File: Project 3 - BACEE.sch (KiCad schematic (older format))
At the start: 13 parts, among them U1 DS1337S, U2 24LC1025, U3 24LC1025, U4 ATMEGA328P-AU, Y1 Crystal 32 MHz, Y2 Crystal 16 MHz

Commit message: Completed wiring in root sheet
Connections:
- net GND is gone; now on net GNDPWR: U4.21 (GND), U4.3 (GND), U4.5 (GND)
- net RESET: now also R2.1
- net SCK: now also D1.2 (A), U1.6 (SCL), U2.6 (SCL), U3.6 (SCL)
- net SDA: now also U1.5 (SDA), U2.5 (SDA), U3.5 (SDA)
- net VCC: now also BT1.1 (+), C3.1, R2.2, U1.3 (INTA), U1.8 (VCC), U2.3 (A2), U2.8 (VCC), U3.3 (A2), U3.8 (VCC), U4.20 (AREF)
- net GNDPWR: now reaches BT1.2 (-)
- net GNDPWR: now also C1.1, C2.1, C3.2, R1.2, U1.4 (GND), U2.4 (GND), U2.7 (WP), U3.4 (GND), U3.7 (WP)
- net at C1.2: now also U4.7 (PB6), Y2.2
- net at C2.2: now also U4.8 (PB7), Y2.1
- net at D1.1 (K): now also R1.1
- net ADDS1: now reaches U3.1 (A0)
- net ADDS1: now also U2.1 (A0), U4.23 (PC0)
- net ADDS2: now reaches U3.2 (A1)
- net ADDS2: now also U2.2 (A1), U4.24 (PC1)
- net SCL: now reaches U4.26 (PC3)
- net at U1.1 (X1): now also Y1.1
- net at U1.2 (X2): now also Y1.2
- no-connect marks 0 -> 1
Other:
- moved on the sheet: C1, C2, C3, D1, R1, R2, U2, U4, Y1, Y2

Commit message: Added power flag symbol.
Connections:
- net SCL: no longer names the net of U4.26 (PC3)
- no-connect marks 1 -> 8
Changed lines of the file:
@@
 	1    0    0    -1
 $EndComp
-Text HLabel 4700 5825 2    50   Input ~ 0
-MISO
 Text Label 4500 5825 2    50   ~ 0
 MISO
-Wire Wire Line
-	4700 5825 4500 5825
 Text Label 5850 2450 2    50   ~ 0
 MISO
@@
 F15 "D7" B R 5850 6900 50
 F16 "D8" B R 5850 7025 50
+F17 "MISO" O L 4700 5825 50
 $EndSheet
 Text Label 4500 5975 2    50   ~ 0
@@
 	6350 925  6450 925
 Wire Wire Line
-	6550 925  6550 1050
-Wire Wire Line
 	6450 1050 6450 925
 Connection ~ 6450 925
@@
 GND
 $Comp
-L power:GNDPWR #PWR?
+L power:GNDPWR #PWR0101
 U 1 1 5F101DCC
 P 4500 7500
-F 0 "#PWR?" H 4500 7300 50  0001 C CNN
+F 0 "#PWR0101" H 4500 7300 50  0001 C CNN
 F 1 "GNDPWR" H 4504 7346 50  0000 C CNN
 F 2 "" H 4500 7450 50  0001 C CNN
@@
 Text Label 5850 3550 2    50   ~ 0
 D2
-Text Label 5850 2950 2    50   ~ 0
-SCL
 Wire Wire Line
 	800  1600 1250 1600
@@
 	800  1600 800  1850
 $Comp
-L power:GNDPWR #PWR?
+L power:GNDPWR #PWR0102
 U 1 1 5F11BB4A
 P 2025 2875
-F 0 "#PWR?" H 2025 2675 50  0001 C CNN
+F 0 "#PWR0102" H 2025 2675 50  0001 C CNN
 F 1 "GNDPWR" H 2029 2721 50  0000 C CNN
 F 2 "" H 2025 2825 50  0001 C CNN
@@
 	3350 5075 3350 4800
 $Comp
-L power:GNDPWR #PWR?
+L power:GNDPWR #PWR0103
 U 1 1 5F12642A
 P 2700 5250
-F 0 "#PWR?" H 2700 5050 50  0001 C CNN
+F 0 "#PWR0103" H 2700 5050 50  0001 C CNN
 F 1 "GNDPWR" H 2704 5096 50  0000 C CNN
 F 2 "" H 2700 5200 50  0001 C CNN
@@
 ADDS2
 $Comp
-L power:GNDPWR #PWR?
+L power:GNDPWR #PWR0104
 U 1 1 5F13096F
 P 8600 3325
-F 0 "#PWR?" H 8600 3125 50  0001 C CNN
+F 0 "#PWR0104" H 8600 3125 50  0001 C CNN
 F 1 "GNDPWR" H 8604 3171 50  0000 C CNN
 F 2 "" H 8600 3275 50  0001 C CNN
@@
 	8900 2575 8900 2725
 Wire Wire Line
-	6450 775  8600 775
+	6450 775  7300 775
 Wire Wire Line
 	8600 775  8600 2575
@@
 	3700 1475 3700 1900
 $Comp
-L power:GNDPWR #PWR?
+L power:GNDPWR #PWR0105
 U 1 1 5F1499FF
 P 3700 2025
-F 0 "#PWR?" H 3700 1825 50  0001 C CNN
+F 0 "#PWR0105" H 3700 1825 50  0001 C CNN
 F 1 "GNDPWR" H 3704 1871 50  0000 C CNN
 F 2 "" H 3700 1975 50  0001 C CNN
@@
 	3700 2025 3700 1900
 Connection ~ 3700 1900
+Wire Wire Line
+	5075 2550 5850 2550
+Wire Wire Line
+	4775 2550 4525 2550
+Wire Wire Line
+	4525 2550 4525 2725
+$Comp
+L power:GNDPWR #PWR0106
+U 1 1 5F161C93
+P 4525 3200
+F 0 "#PWR0106" H 4525 3000 50  0001 C CNN
+F 1 "GNDPWR" H 4529 3046 50  0000 C CNN
+F 2 "" H 4525 3150 50  0001 C CNN
+F 3 "" H 4525 3150 50  0001 C CNN
+	1    4525 3200
+	1    0    0    -1
+$EndComp
+Wire Wire Line
+	4525 3200 4525 3025
+Wire Wire Line
+	5850 3250 5275 3250
+Text Label 4975 3775 2    50   ~ 0
+VCC
+Wire Wire Line
+	5275 3550 5275 3750
+Wire Wire Line
+	5275 3775 4975 3775
+Wire Wire Line
+	5850 3750 5275 3750
+Connection ~ 5275 3750
+Wire Wire Line
+	5275 3750 5275 3775
+$Comp
+L power:GNDPWR #PWR0107
+U 1 1 5F16FCAB
+P 6450 4625
+F 0 "#PWR0107" H 6450 4425 50  0001 C CNN
+F 1 "GNDPWR" H 6454 4471 50  0000 C CNN
+F 2 "" H 6450 4575 50  0001 C CNN
+F 3 "" H 6450 4575 50  0001 C CNN
+	1    6450 4625
+	1    0    0    -1
+$EndComp
+Wire Wire Line
+	6450 4300 6450 4625
+NoConn ~ 5850 3850
+NoConn ~ 5850 3650
+NoConn ~ 5850 3150
+NoConn ~ 5850 2850
+NoConn ~ 5850 2250
+NoConn ~ 5850 2150
+Wire Wire Line
+	4700 5825 4500 5825
+Wire Wire Line
+	6550 925  6550 1050
+NoConn ~ 5850 2950
 $Comp
 L dk_Embedded-Microcontrollers:ATMEGA328P-AU U4
@@
 	1    0    0    -1
 $EndComp
-Wire Wire Line
-	5075 2550 5850 2550
-Wire Wire Line
-	4775 2550 4525 2550
-Wire Wire Line
-	4525 2550 4525 2725
-$Comp
-L power:GNDPWR #PWR?
-U 1 1 5F161C93
-P 4525 3200
-F 0 "#PWR?" H 4525 3000 50  0001 C CNN
-F 1 "GNDPWR" H 4529 3046 50  0000 C CNN
-F 2 "" H 4525 3150 50  0001 C CNN
-F 3 "" H 4525 3150 50  0001 C CNN
-	1    4525 3200
-	1    0    0    -1
-$EndComp
-Wire Wire Line
-	4525 3200 4525 3025
-Wire Wire Line
-	5850 3250 5275 3250
-Text Label 4975 3775 2    50   ~ 0
-VCC
-Wire Wire Line
-	5275 3550 5275 3750
-Wire Wire Line
-	5275 3775 4975 3775
-Wire Wire Line
-	5850 3750 5275 3750
-Connection ~ 5275 3750
-Wire Wire Line
-	5275 3750 5275 3775
-$Comp
-L power:GNDPWR #PWR?
-U 1 1 5F16FCAB
-P 6450 4625
-F 0 "#PWR?" H 6450 4425 50  0001 C CNN
-F 1 "GNDPWR" H 6454 4471 50  0000 C CNN
-F 2 "" H 6450 4575 50  0001 C CNN
-F 3 "" H 6450 4575 50  0001 C CNN
-	1    6450 4625
-	1    0    0    -1
-$EndComp
-Wire Wire Line
-	6450 4300 6450 4625
+$Comp
+L power:PWR_FLAG #FLG0101
+U 1 1 5F1973DA
+P 7300 700
+F 0 "#FLG0101" H 7300 775 50  0001 C CNN
+F 1 "PWR_FLAG" H 7300 873 50  0000 C CNN
+F 2 "" H 7300 700 50  0001 C CNN
+F 3 "~" H 7300 700 50  0001 C CNN
+	1    7300 700
+	1    0    0    -1
+$EndComp
+Wire Wire Line
+	7300 700  7300 775
+Connection ~ 7300 775
+Wire Wire Line
+	7300 775  8600 775
 $EndSCHEMATC

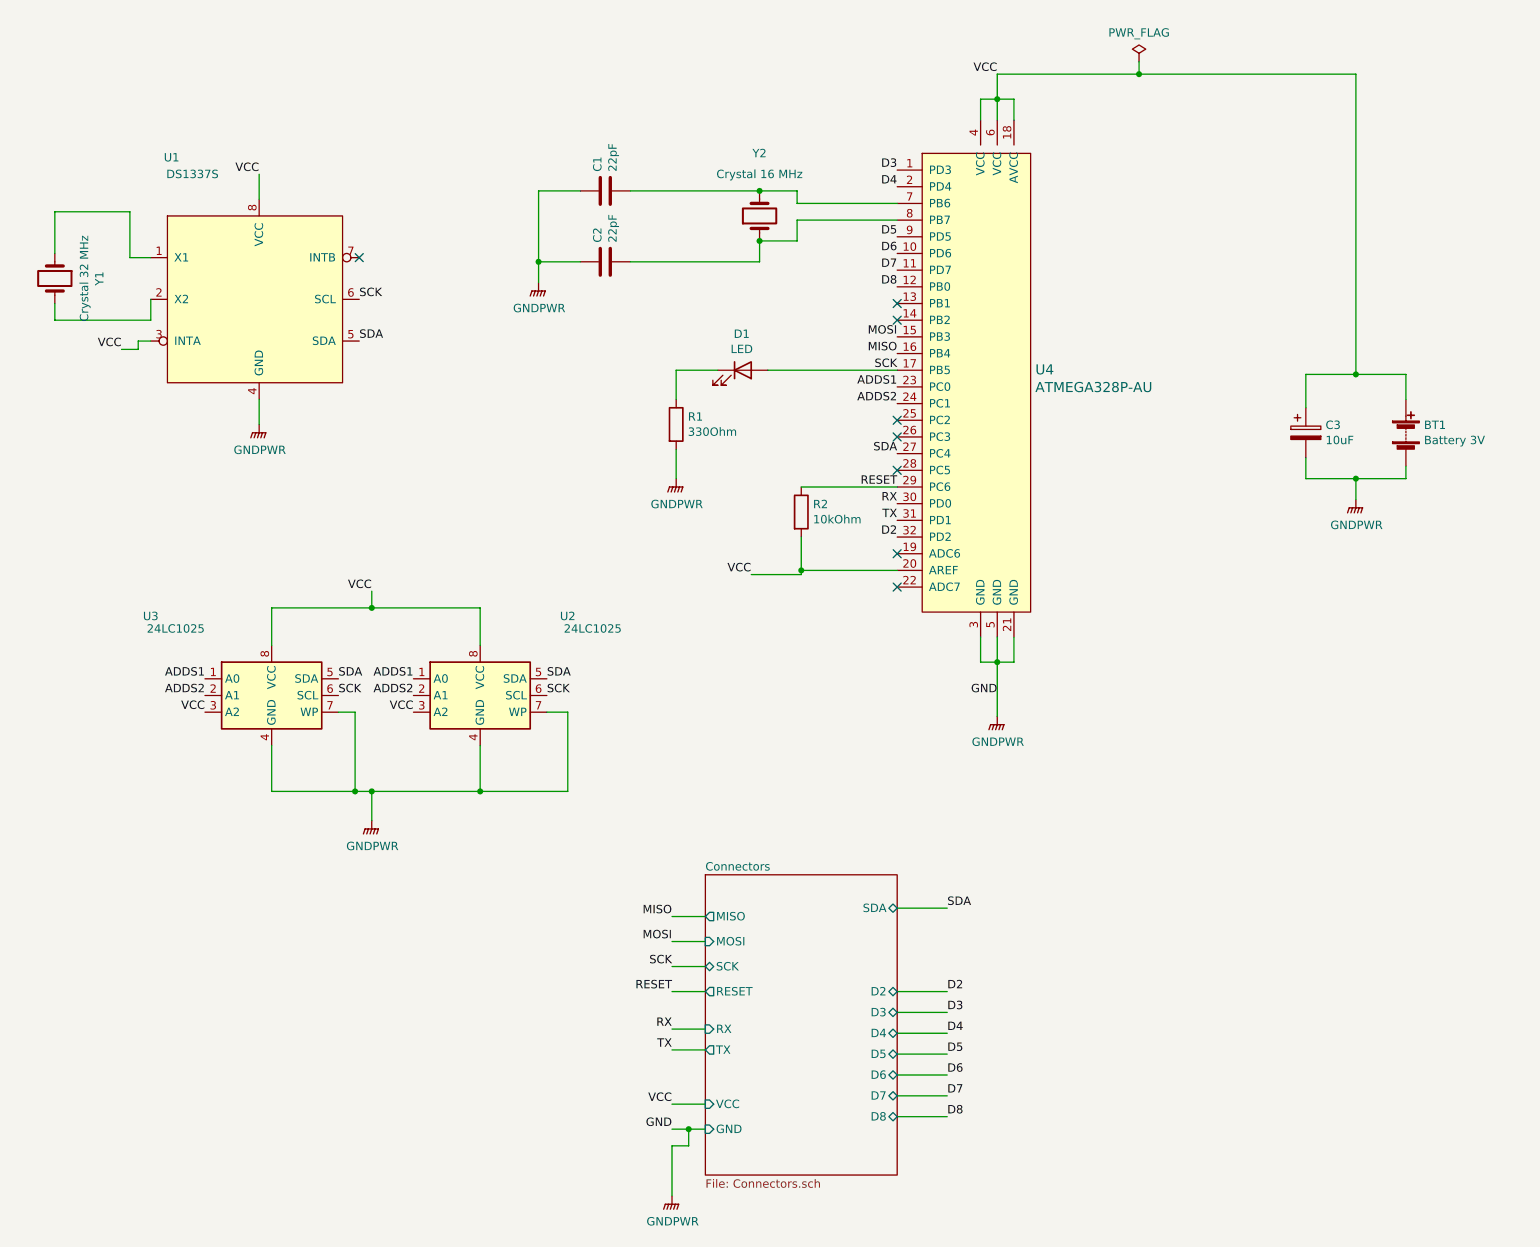
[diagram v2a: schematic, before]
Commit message: Added functional block descriptions.
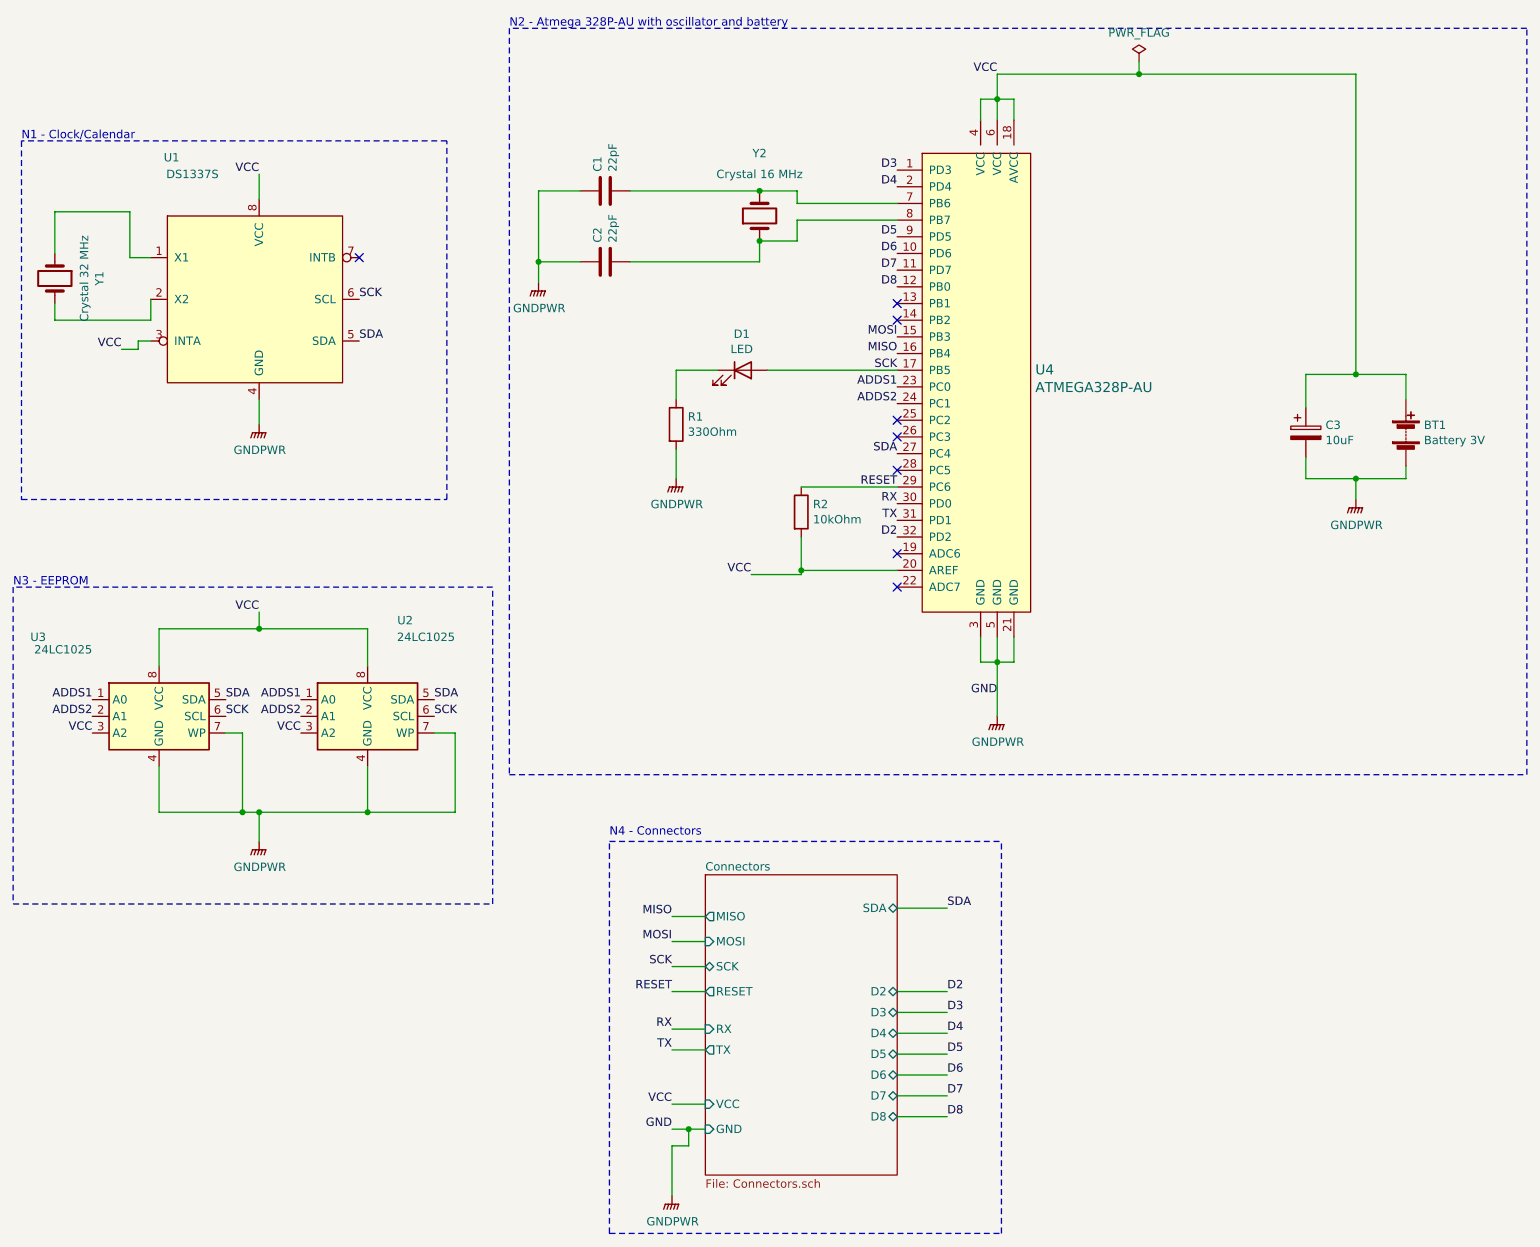
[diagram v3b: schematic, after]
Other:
- note added: "N1 - Clock/Calendar"
- note added: "N2 - Atmega 328P-AU with oscillator and battery"
- note added: "N3 - EEPROM"
- note added: "N4 - Connectors"
- moved on the sheet: U2, U3
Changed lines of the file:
@@
 L Memory_EEPROM:24LC1025 U3
 U 1 1 5F0D1B59
-P 2100 4500
-F 0 "U3" H 1375 4975 50  0000 C CNN
-F 1 "24LC1025" H 1525 4900 50  0000 C CNN
-F 2 "Package_SO:SOIJ-8_5.3x5.3mm_P1.27mm" H 2100 4500 50  0001 C CNN
-F 3 "http://ww1.microchip.com/downloads/en/DeviceDoc/21941B.pdf" H 2100 4500 50  0001 C CNN
-	1    2100 4500
+P 1425 4625
+F 0 "U3" H 700 5100 50  0000 C CNN
+F 1 "24LC1025" H 850 5025 50  0000 C CNN
+F 2 "Package_SO:SOIJ-8_5.3x5.3mm_P1.27mm" H 1425 4625 50  0001 C CNN
+F 3 "http://ww1.microchip.com/downloads/en/DeviceDoc/21941B.pdf" H 1425 4625 50  0001 C CNN
+	1    1425 4625
 	1    0    0    -1
 $EndComp
@@
 L Memory_EEPROM:24LC1025 U2
 U 1 1 5F0EDBCB
-P 3350 4500
-F 0 "U2" H 3875 4975 50  0000 C CNN
-F 1 "24LC1025" H 4025 4900 50  0000 C CNN
-F 2 "Package_SO:SOIJ-8_5.3x5.3mm_P1.27mm" H 3350 4500 50  0001 C CNN
-F 3 "http://ww1.microchip.com/downloads/en/DeviceDoc/21941B.pdf" H 3350 4500 50  0001 C CNN
-	1    3350 4500
+P 2675 4625
+F 0 "U2" H 2900 5200 50  0000 C CNN
+F 1 "24LC1025" H 3025 5100 50  0000 C CNN
+F 2 "Package_SO:SOIJ-8_5.3x5.3mm_P1.27mm" H 2675 4625 50  0001 C CNN
+F 3 "http://ww1.microchip.com/downloads/en/DeviceDoc/21941B.pdf" H 2675 4625 50  0001 C CNN
+	1    2675 4625
 	1    0    0    -1
 $EndComp
@@
 Text Label 2625 2375 0    50   ~ 0
 SDA
-Text Label 2700 3875 2    50   ~ 0
-VCC
-Wire Wire Line
-	2100 4200 2100 3975
-Wire Wire Line
-	2100 3975 2700 3975
-Wire Wire Line
-	3350 3975 3350 4200
-Wire Wire Line
-	2700 3875 2700 3975
-Connection ~ 2700 3975
-Wire Wire Line
-	2700 3975 3350 3975
-Wire Wire Line
-	2100 4800 2100 5075
-Wire Wire Line
-	2100 5075 2600 5075
-Wire Wire Line
-	3350 5075 3350 4800
+Text Label 2025 4000 2    50   ~ 0
+VCC
+Wire Wire Line
+	1425 4325 1425 4100
+Wire Wire Line
+	1425 4100 2025 4100
+Wire Wire Line
+	2675 4100 2675 4325
+Wire Wire Line
+	2025 4000 2025 4100
+Connection ~ 2025 4100
+Wire Wire Line
+	2025 4100 2675 4100
+Wire Wire Line
+	1425 4925 1425 5200
+Wire Wire Line
+	1425 5200 1925 5200
+Wire Wire Line
+	2675 5200 2675 4925
 $Comp
 L power:GNDPWR #PWR0103
 U 1 1 5F12642A
-P 2700 5250
-F 0 "#PWR0103" H 2700 5050 50  0001 C CNN
-F 1 "GNDPWR" H 2704 5096 50  0000 C CNN
-F 2 "" H 2700 5200 50  0001 C CNN
-F 3 "" H 2700 5200 50  0001 C CNN
-	1    2700 5250
-	1    0    0    -1
-$EndComp
-Wire Wire Line
-	2700 5250 2700 5075
-Connection ~ 2700 5075
-Wire Wire Line
-	2700 5075 3350 5075
-Wire Wire Line
-	2500 4600 2600 4600
-Wire Wire Line
-	2600 4600 2600 5075
-Connection ~ 2600 5075
-Wire Wire Line
-	2600 5075 2700 5075
-Wire Wire Line
-	3750 4600 3875 4600
-Wire Wire Line
-	3875 4600 3875 5075
-Wire Wire Line
-	3875 5075 3350 5075
-Connection ~ 3350 5075
-Text Label 1700 4600 2    50   ~ 0
-VCC
-Text Label 2950 4600 2    50   ~ 0
-VCC
-Text Label 2500 4400 0    50   ~ 0
+P 2025 5375
+F 0 "#PWR0103" H 2025 5175 50  0001 C CNN
+F 1 "GNDPWR" H 2029 5221 50  0000 C CNN
+F 2 "" H 2025 5325 50  0001 C CNN
+F 3 "" H 2025 5325 50  0001 C CNN
+	1    2025 5375
+	1    0    0    -1
+$EndComp
+Wire Wire Line
+	2025 5375 2025 5200
+Connection ~ 2025 5200
+Wire Wire Line
+	2025 5200 2675 5200
+Wire Wire Line
+	1825 4725 1925 4725
+Wire Wire Line
+	1925 4725 1925 5200
+Connection ~ 1925 5200
+Wire Wire Line
+	1925 5200 2025 5200
+Wire Wire Line
+	3075 4725 3200 4725
+Wire Wire Line
+	3200 4725 3200 5200
+Wire Wire Line
+	3200 5200 2675 5200
+Connection ~ 2675 5200
+Text Label 1025 4725 2    50   ~ 0
+VCC
+Text Label 2275 4725 2    50   ~ 0
+VCC
+Text Label 1825 4525 0    50   ~ 0
 SDA
-Text Label 2500 4500 0    50   ~ 0
+Text Label 1825 4625 0    50   ~ 0
 SCK
-Text Label 3750 4500 0    50   ~ 0
+Text Label 3075 4625 0    50   ~ 0
 SCK
-Text Label 3750 4400 0    50   ~ 0
+Text Label 3075 4525 0    50   ~ 0
 SDA
-Text Label 1700 4400 2    50   ~ 0
+Text Label 1025 4525 2    50   ~ 0
 ADDS1
-Text Label 2950 4400 2    50   ~ 0
+Text Label 2275 4525 2    50   ~ 0
 ADDS1
-Text Label 1700 4500 2    50   ~ 0
+Text Label 1025 4625 2    50   ~ 0
 ADDS2
-Text Label 2950 4500 2    50   ~ 0
+Text Label 2275 4625 2    50   ~ 0
 ADDS2
 Text Label 5850 2650 2    50   ~ 0
@@
 Wire Wire Line
 	7300 775  8600 775
+Wire Notes Line
+	600  1175 600  3325
+Wire Notes Line
+	600  3325 3150 3325
+Wire Notes Line
+	3150 3325 3150 1175
+Wire Notes Line
+	3150 1175 600  1175
+Wire Notes Line
+	4125 7725 6475 7725
+Wire Notes Line
+	6475 7725 6475 5375
+Wire Notes Line
+	4125 7725 4125 5375
+Wire Notes Line
+	4125 5375 6475 5375
+Wire Notes Line
+	550  3850 550  5750
+Wire Notes Line
+	9625 4975 9625 500
+Wire Notes Line
+	9625 500  3525 500
+Wire Notes Line
+	3525 500  3525 4975
+Wire Notes Line
+	3525 4975 9625 4975
+Wire Notes Line
+	550  5750 3425 5750
+Wire Notes Line
+	3425 5750 3425 3850
+Wire Notes Line
+	3425 3850 550  3850
+Text Notes 600  1175 0    50   ~ 0
+N1 - Clock/Calendar
+Text Notes 550  3850 0    50   ~ 0
+N3 - EEPROM
+Text Notes 3525 500  0    50   ~ 0
+N2 - Atmega 328P-AU with oscillator and battery
+Text Notes 4125 5350 0    50   ~ 0
+N4 - Connectors
 $EndSCHEMATC
